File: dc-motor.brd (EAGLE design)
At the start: 160 x 100 mm, 82 parts, among them IC1 MEGA32-A, X3 RIA_3POL, X4 RIA_3POL, X5 RIA_2POL, X6 JUMP1-4, X8 PFVERB10

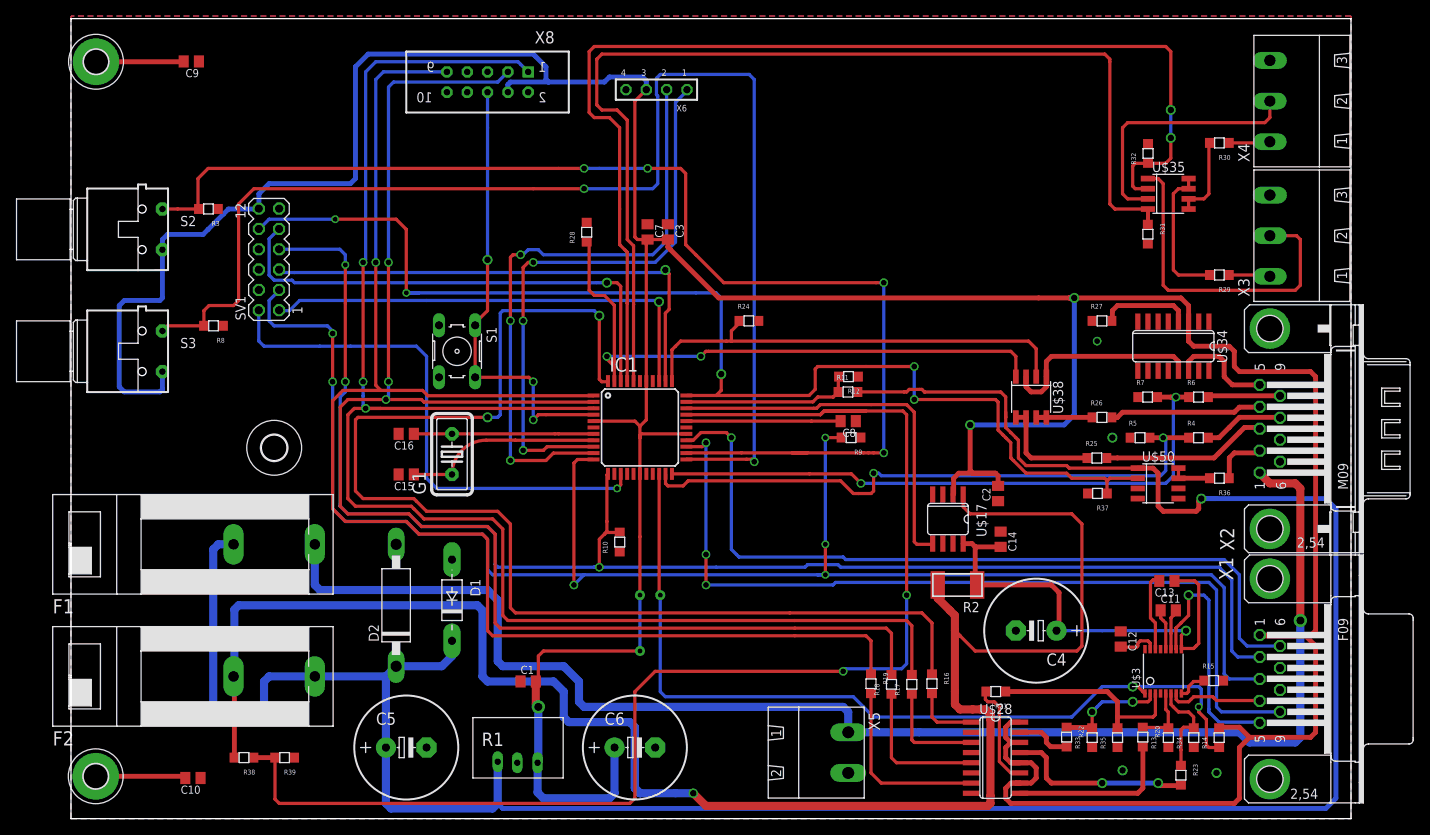
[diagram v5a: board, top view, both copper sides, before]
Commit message: Pull Down resistor added
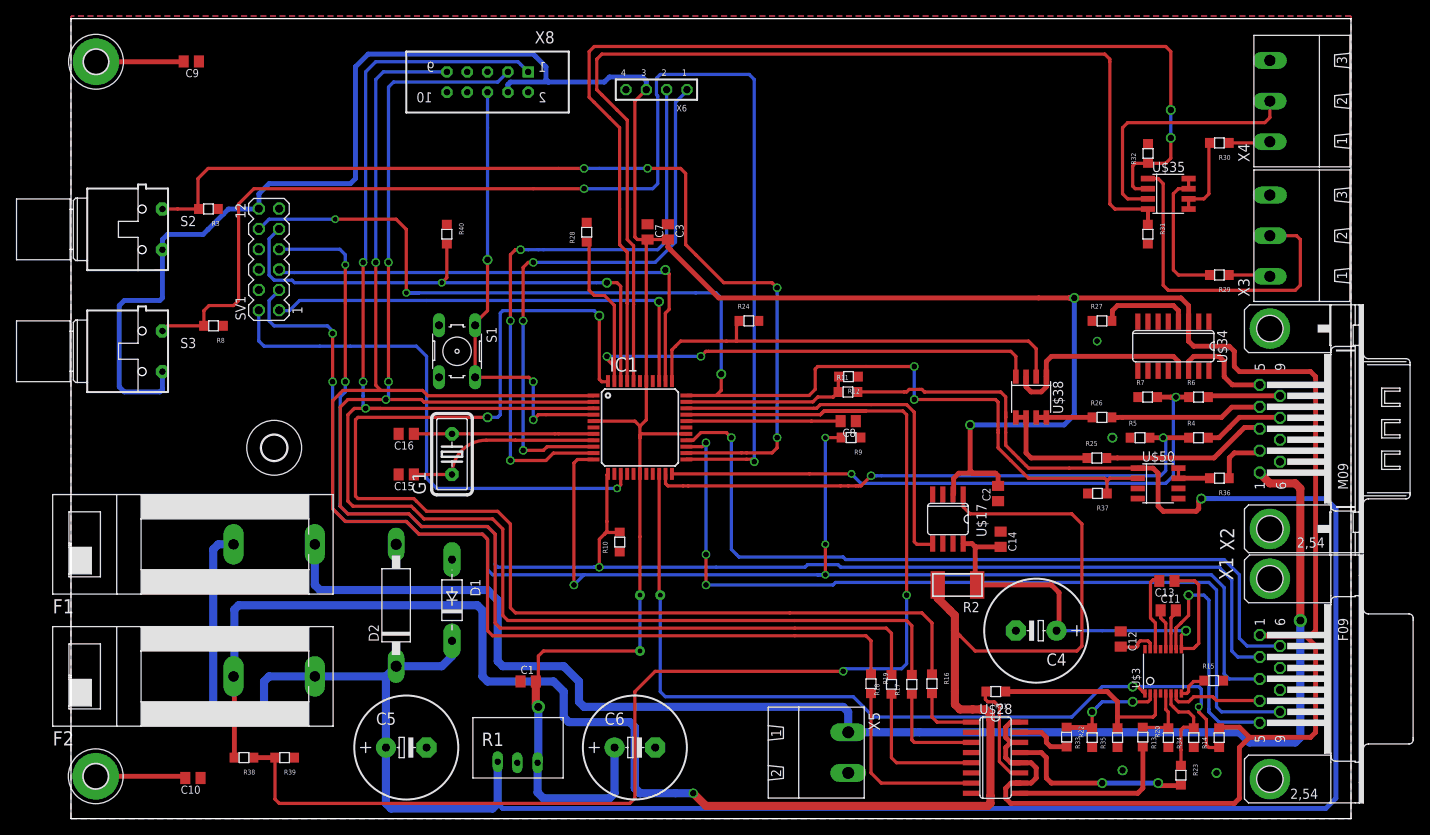
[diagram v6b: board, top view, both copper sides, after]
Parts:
- added R40: 2k7, Resistor:0805
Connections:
- net GND: now also R40.1, U$3.16
- net MOTORSTOP: now also R40.2
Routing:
- net N$17: track 153.8 -> 124.5 mm
- net MOTORSTOP: track 62.7 -> 67.8 mm, vias 1 -> 2
- net N$9: track 78.4 -> 75.5 mm
- net ENDLAGE_B: track 134.9 -> 133.8 mm
- net ENDLAGE_A: track 140.6 -> 139.5 mm

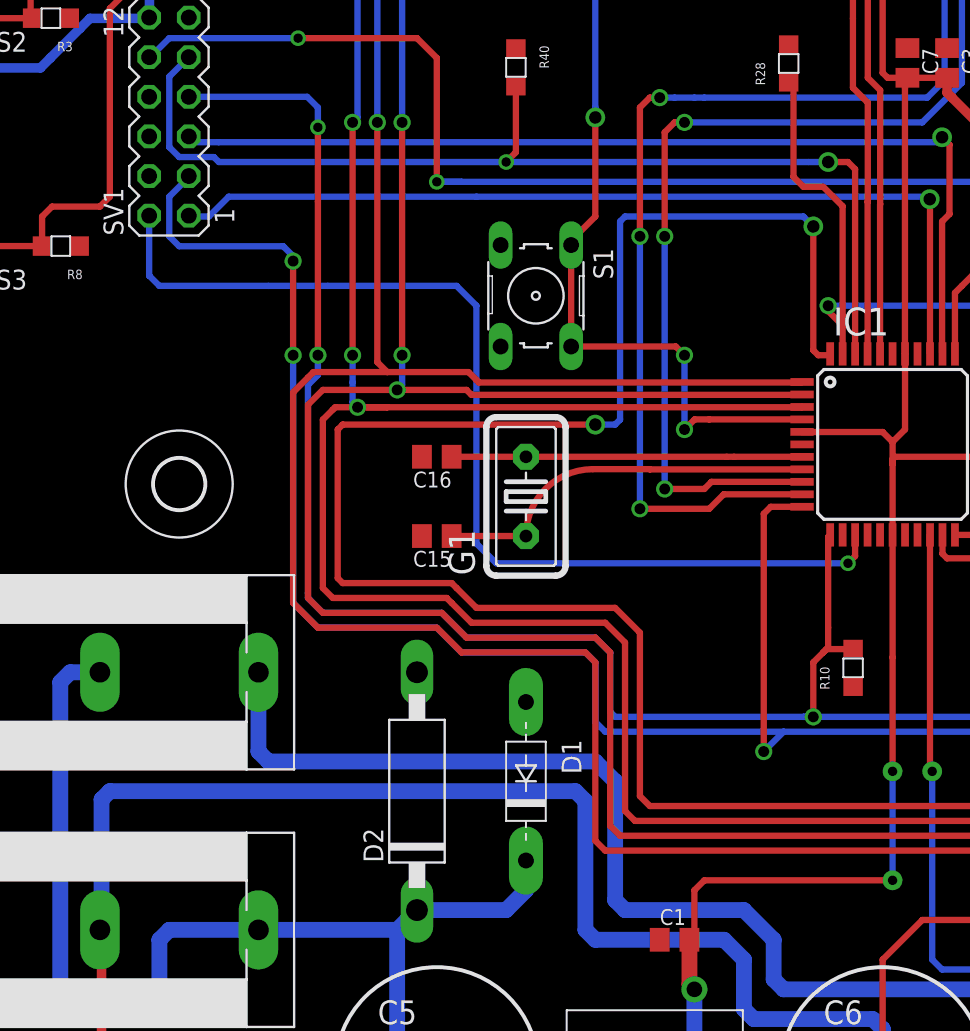
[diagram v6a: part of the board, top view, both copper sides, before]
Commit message: PWR_LED Connected
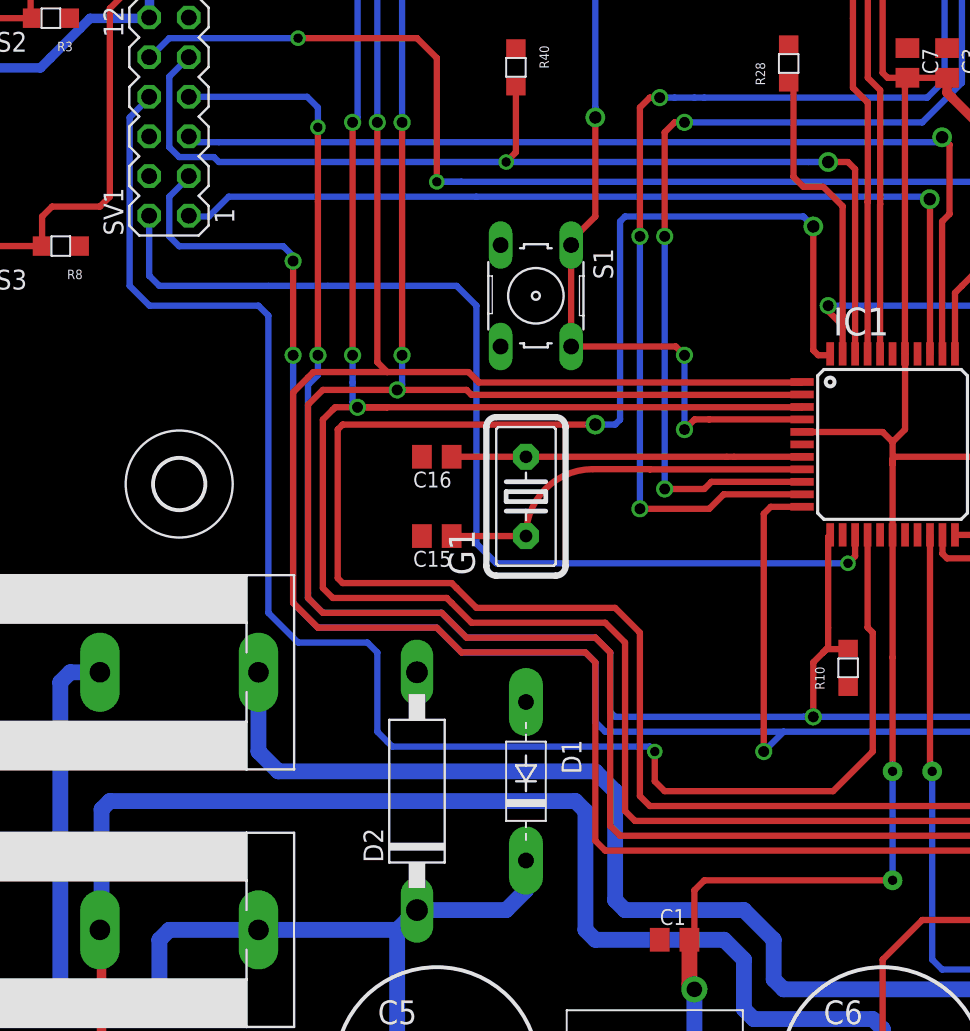
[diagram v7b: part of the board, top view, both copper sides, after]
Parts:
- moved R10 0.32 mm to (68.9, 34.0)
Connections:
- net +24V_LED_µC: now also IC1.15
- net GND: no longer IC1.15
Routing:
- net +24V_LED_µC: track 0.00 -> 104.0 mm, vias 0 -> 1
- net N$6: track 227.7 -> 226.4 mm
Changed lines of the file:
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@@
 <element name="C4" library="Capacitor" package="E5-13" value="100µF/50V" x="120.65" y="23.495" rot="R180"/>
 <element name="R9" library="Resistor" package="0805" value="2k7" x="98.1075" y="48.26" rot="R180"/>
-<element name="R10" library="Resistor" package="0805" value="2k7" x="69.215" y="33.9725" rot="R90"/>
+<element name="R10" library="Resistor" package="0805" value="2k7" x="68.8975" y="33.9725" rot="R90"/>
 <element name="H1" library="Holes" package="3,0-PAD" value="MOUNT-PAD-ROUND3.0" x="3.13" y="94.61"/>
 <element name="H2" library="Holes" package="3,0-PAD" value="MOUNT-PAD-ROUND3.0" x="3.095" y="5.295"/>
@@
 <contactref element="IC1" pad="37"/>
 <contactref element="IC1" pad="16"/>
-<contactref element="IC1" pad="15"/>
 <contactref element="U$3" pad="16"/>
 <contactref element="R40" pad="1"/>
@@
 <contactref element="F1" pad="2"/>
 <wire x1="30.48" y1="34.29" x2="30.48" y2="29.21" width="1.016" layer="16"/>
-<wire x1="30.48" y1="29.21" x2="31.115" y2="28.575" width="1.016" layer="16"/>
-<wire x1="31.115" y1="28.575" x2="52.07" y2="28.575" width="1.016" layer="16"/>
-<wire x1="52.07" y1="28.575" x2="53.34" y2="27.305" width="1.016" layer="16"/>
-<wire x1="53.34" y1="27.305" x2="53.34" y2="19.685" width="1.016" layer="16"/>
+<wire x1="30.48" y1="29.21" x2="31.75" y2="27.94" width="1.016" layer="16"/>
+<wire x1="31.75" y1="27.94" x2="52.07" y2="27.94" width="1.016" layer="16"/>
+<wire x1="52.07" y1="27.94" x2="53.34" y2="26.67" width="1.016" layer="16"/>
+<wire x1="53.34" y1="26.67" x2="53.34" y2="19.685" width="1.016" layer="16"/>
 <wire x1="53.34" y1="19.685" x2="53.975" y2="19.05" width="1.016" layer="16"/>
 <wire x1="53.975" y1="19.05" x2="61.595" y2="19.05" width="1.016" layer="16"/>
@@
 <contactref element="F2" pad="1"/>
 <contactref element="R38" pad="2"/>
-<wire x1="20.4239" y1="26.1389" x2="20.955" y2="26.67" width="1.016" layer="16"/>
-<wire x1="20.955" y1="26.67" x2="50.8" y2="26.67" width="1.016" layer="16"/>
-<wire x1="50.8" y1="26.67" x2="51.435" y2="26.035" width="1.016" layer="16"/>
-<wire x1="51.435" y1="26.035" x2="51.435" y2="17.78" width="1.016" layer="16"/>
+<wire x1="20.4239" y1="25.5039" x2="20.955" y2="26.035" width="1.016" layer="16"/>
+<wire x1="20.955" y1="26.035" x2="50.8" y2="26.035" width="1.016" layer="16"/>
+<wire x1="50.8" y1="26.035" x2="51.435" y2="25.4" width="1.016" layer="16"/>
+<wire x1="51.435" y1="25.4" x2="51.435" y2="17.78" width="1.016" layer="16"/>
 <wire x1="51.435" y1="17.78" x2="52.07" y2="17.145" width="1.016" layer="16"/>
 <wire x1="52.07" y1="17.145" x2="60.325" y2="17.145" width="1.016" layer="16"/>
@@
 <wire x1="114.3" y1="13.6525" x2="114.935" y2="13.0175" width="1.016" layer="1"/>
 <wire x1="114.935" y1="13.0175" x2="114.935" y2="12.3825" width="1.016" layer="1"/>
-<wire x1="20.4239" y1="26.1389" x2="20.4239" y2="17.8839" width="1.016" layer="16"/>
+<wire x1="20.4239" y1="25.5039" x2="20.4239" y2="17.8839" width="1.016" layer="16"/>
 <wire x1="20.4239" y1="17.8839" x2="20.32" y2="17.78" width="1.016" layer="16"/>
 <wire x1="20.4239" y1="7.6305" x2="20.4239" y2="17.6761" width="0.6096" layer="1"/>
@@
 <wire x1="66.9925" y1="37.1475" x2="66.9925" y2="42.9675" width="0.4064" layer="1"/>
 <wire x1="66.9925" y1="42.9675" x2="67.12" y2="43.095" width="0.4064" layer="1"/>
-<wire x1="68.5905" y1="35.7736" x2="66.8886" y2="35.7736" width="0.4064" layer="1"/>
+<wire x1="68.273" y1="35.7736" x2="66.8886" y2="35.7736" width="0.4064" layer="1"/>
 <wire x1="66.8886" y1="35.7736" x2="66.675" y2="35.56" width="0.4064" layer="1"/>
 <wire x1="66.675" y1="35.56" x2="66.04" y2="34.925" width="0.4064" layer="1"/>
@@
 <signal name="+24V_LED_µC">
 <contactref element="SV1" pad="8"/>
+<contactref element="IC1" pad="15"/>
+<wire x1="23.474" y1="71.173" x2="23.474" y2="71.099" width="0.4064" layer="16"/>
+<wire x1="23.474" y1="71.099" x2="22.225" y2="69.85" width="0.4064" layer="16"/>
+<wire x1="22.225" y1="69.85" x2="22.225" y2="59.055" width="0.4064" layer="16"/>
+<wire x1="22.225" y1="59.055" x2="23.495" y2="57.785" width="0.4064" layer="16"/>
+<wire x1="23.495" y1="57.785" x2="30.48" y2="57.785" width="0.4064" layer="16"/>
+<wire x1="30.48" y1="57.785" x2="31.115" y2="57.15" width="0.4064" layer="16"/>
+<wire x1="31.115" y1="57.15" x2="31.115" y2="38.1" width="0.4064" layer="16"/>
+<wire x1="31.115" y1="38.1" x2="33.02" y2="36.195" width="0.4064" layer="16"/>
+<wire x1="33.02" y1="36.195" x2="37.465" y2="36.195" width="0.4064" layer="16"/>
+<wire x1="37.465" y1="36.195" x2="38.1" y2="35.56" width="0.4064" layer="16"/>
+<wire x1="38.1" y1="35.56" x2="38.1" y2="30.48" width="0.4064" layer="16"/>
+<wire x1="38.1" y1="30.48" x2="38.735" y2="29.845" width="0.4064" layer="16"/>
+<wire x1="69.52" y1="43.095" x2="69.52" y2="37.16" width="0.4064" layer="1"/>
+<wire x1="69.52" y1="37.16" x2="69.85" y2="36.83" width="0.4064" layer="1"/>
+<wire x1="56.515" y1="26.67" x2="55.88" y2="27.305" width="0.4064" layer="1"/>
+<wire x1="55.88" y1="27.305" x2="55.88" y2="29.21" width="0.4064" layer="1"/>
+<via x="55.88" y="29.21" extent="1-16" drill="0.6" shape="octagon"/>
+<wire x1="55.88" y1="29.21" x2="55.5625" y2="29.5275" width="0.4064" layer="16"/>
+<wire x1="55.5625" y1="29.5275" x2="39.0525" y2="29.5275" width="0.4064" layer="16"/>
+<wire x1="39.0525" y1="29.5275" x2="38.735" y2="29.845" width="0.4064" layer="16"/>
+<wire x1="56.515" y1="26.67" x2="67.31" y2="26.67" width="0.4064" layer="1"/>
+<wire x1="67.31" y1="26.67" x2="69.85" y2="29.21" width="0.4064" layer="1"/>
+<wire x1="69.85" y1="29.21" x2="69.85" y2="36.83" width="0.4064" layer="1"/>
 </signal>
 <signal name="N$20">

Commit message: just weired
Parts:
- moved R9 39.2 mm to (59.4, 42.2), turned to 0 degrees
- moved R10 3.81 mm to (65.1, 34.0)
- moved C3 0.64 mm to (75.2, 73.3)
- moved S1 0.64 mm to (48.9, 58.4)
- moved C7 0.63 mm to (72.7, 73.3)
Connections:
- new net ENDSCHALTERA: IC1.11, R9.2, X1.3
- new net ENDSCHALTERB: IC1.12, R10.2, X1.2
- net ENDSCHALTER_A: now also IC1.13; no longer IC1.11, R9.2, X1.3
- net ENDSCHALTER_B: now also IC1.16; no longer IC1.12, R10.2, X1.2
- net GND: no longer IC1.13, IC1.16
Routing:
- net ENDSCHALTER_A: track 208.1 -> 69.7 mm, vias 6 -> 1
- net ENDSCHALTERB: track 0.00 -> 118.2 mm, vias 0 -> 1
- net ENDSCHALTERA: track 0.00 -> 117.8 mm, vias 0 -> 1
- net ENDSCHALTER_B: track 185.4 -> 100.7 mm
- net ERROR_LED: track 67.2 -> 70.2 mm
- net +24V_LED_µC: track 104.0 -> 101.0 mm
- net LOCAL/REMOTE: track 153.9 -> 152.3 mm
- net RESET: track 56.3 -> 55.4 mm
- net N$17: track 124.5 -> 125.2 mm
